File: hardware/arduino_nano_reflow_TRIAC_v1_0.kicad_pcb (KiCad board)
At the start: 2 copper layers, 100 x 50 mm, 36 parts, among them J1 AC IN 220v, J10 CONN_01X17, J11 CONN_01X03, J12 MOUNTING_HOLE, J13 MOUNTING_HOLE, J14 MOUNTING_HOLE, J15 MOUNTING_HOLE, J2 HEATER, J3 DC IN 12V, J4 12v FAN, J5 CONN_01X03, J6 CONN_01X03, J7 CONN_01X03, J8 CONN_01X03, J9 CONN_01X05, Q1 IRF540N, U1 MOC3020M

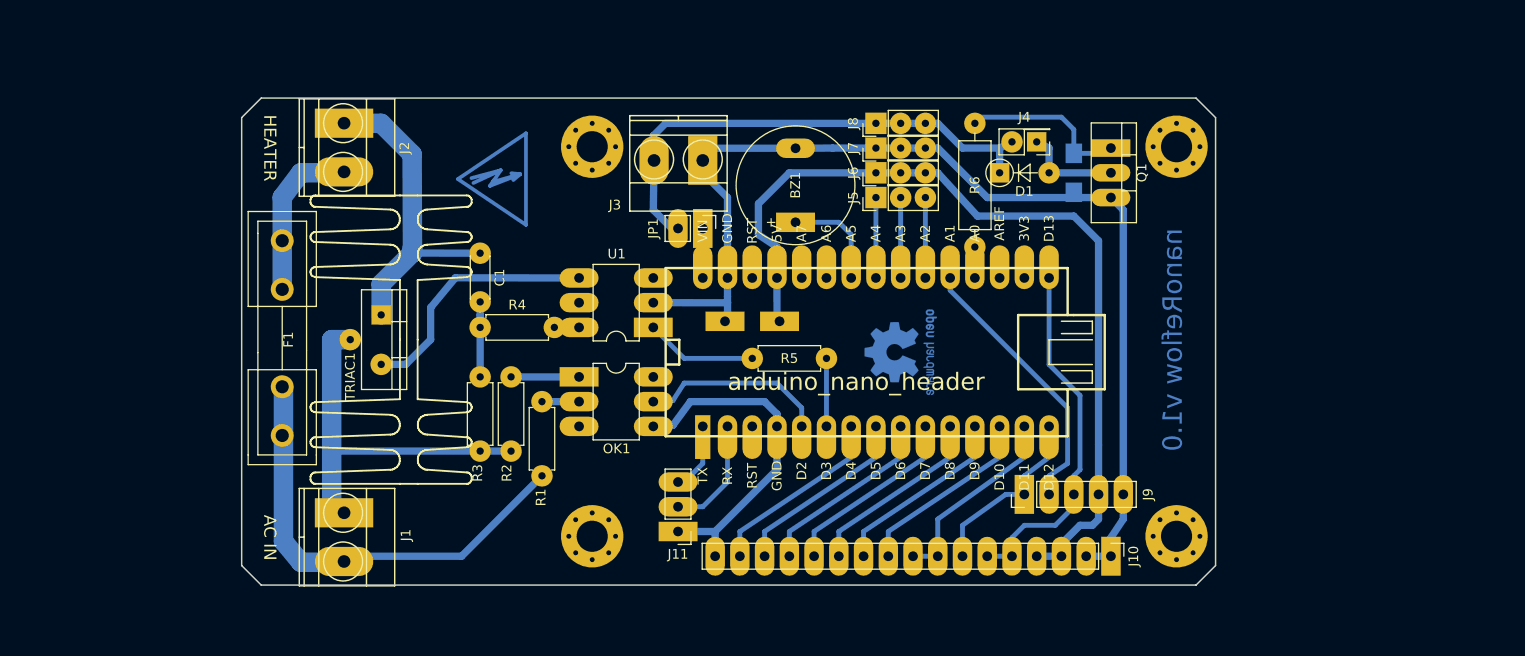
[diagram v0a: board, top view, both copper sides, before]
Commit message: Big update. Lots of schematic reorg and mostly final PCB layout. Updated zero crossing detector to be more accurate and added temp sensor on board instead of a connector to a separate module. Moved some pins around on the micro for better layout. Added safety ground to mains input.
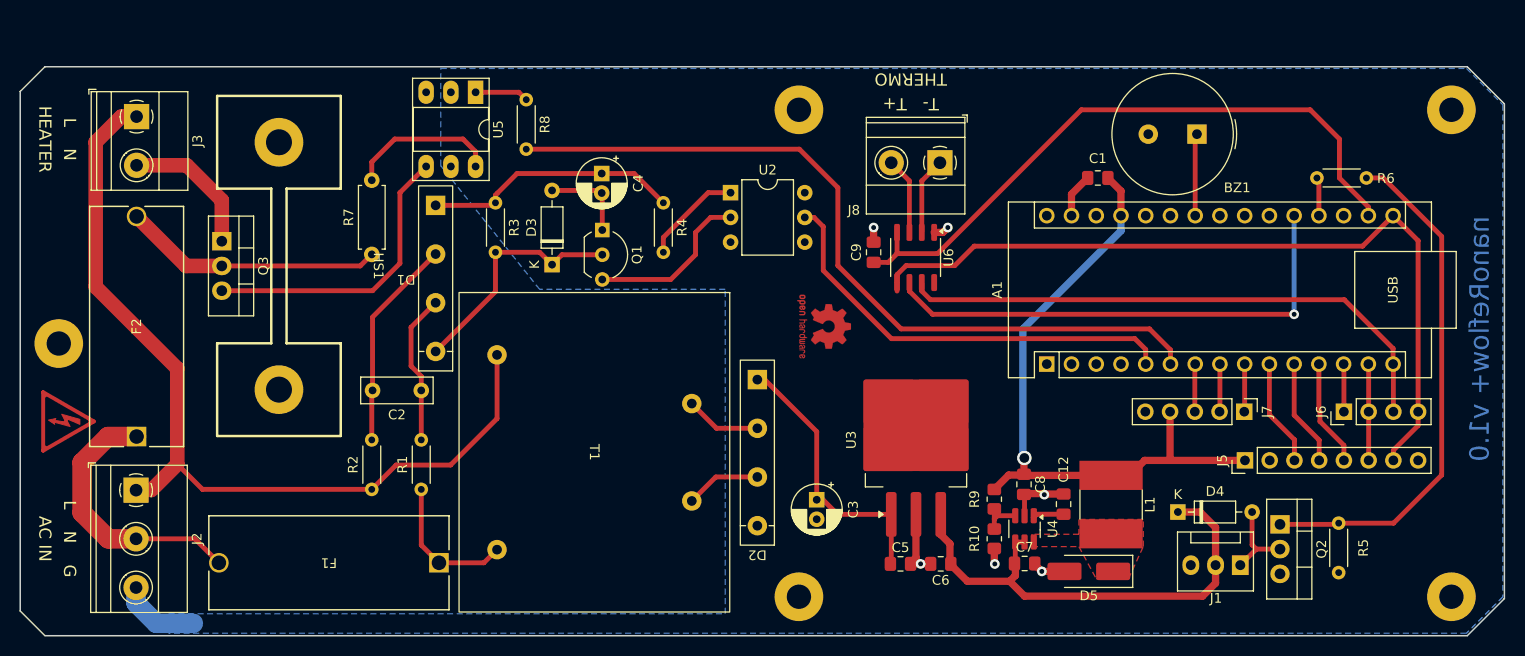
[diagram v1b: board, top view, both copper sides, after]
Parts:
- removed ARDUINO_NANO1: arduino_nano_header, local_modules:arduino_nano_header
- removed J10: CONN_01X17, Pin_Headers:Pin_Header_Straight_1x17_Pitch2.54mm
- removed J11: CONN_01X03, Pin_Headers:Pin_Header_Straight_1x03_Pitch2.54mm
- removed J12, J13, J14, J15: MOUNTING_HOLE, Mounting_Holes:MountingHole_3.2mm_M3_Pad_Via
- removed the J3 at (147.8, 74.4)
- removed J4: 12v FAN, Pin_Headers:Pin_Header_Straight_2x01_Pitch2.54mm
- removed J9: CONN_01X05, Pin_Headers:Pin_Header_Straight_1x05_Pitch2.54mm
- removed JP1: VIN enabler, Pin_Headers:Pin_Header_Straight_1x02_Pitch2.54mm
- removed KK1: TRIAC HEATSINK, local_modules:TO_220_heatsink
- removed OK1: H11AA1, Housings_DIP:DIP-6_W7.62mm_LongPads
- removed the R7 at (185.9, 75.7)
- removed U1: MOC3020M, Housings_DIP:DIP-6_W7.62mm_LongPads
- added A1: Arduino_Nano_Every, Module:Arduino_Nano, F.Cu at (183.2, 95.3)
- added C12: 0.01uF, Capacitor_SMD:C_0805_2012Metric_Pad1.18x1.45mm_HandSolder, F.Cu at (184.9, 109.7)
- added C3: 10uF, Capacitor_THT:CP_Radial_D5.0mm_P2.00mm, F.Cu at (159.5, 109.2)
- added C4: 10uF 10V, Capacitor_THT:CP_Radial_D5.0mm_P2.00mm, F.Cu at (137.5, 75.7)
- added C5: 0.22uF, Capacitor_SMD:C_0805_2012Metric_Pad1.18x1.45mm_HandSolder, F.Cu at (168.1, 115.8)
- added C6: 0.1uF, Capacitor_SMD:C_0805_2012Metric_Pad1.18x1.45mm_HandSolder, F.Cu at (172.3, 115.8)
- added C7: 0.1uF, Capacitor_SMD:C_0805_2012Metric_Pad1.18x1.45mm_HandSolder, F.Cu at (180.9, 115.8)
- added C8: 10uF, Capacitor_SMD:C_0805_2012Metric_Pad1.18x1.45mm_HandSolder, F.Cu at (180.8, 107.7)
- added C9: 0.1 uF 6.3 V, Capacitor_SMD:C_0805_2012Metric_Pad1.18x1.45mm_HandSolder, F.Cu at (165.4, 83.8)
- added D2: B40C1500A, arduino_nano_reflow:B40C, F.Cu at (153.5, 104.4)
- added D3: 1N4148, Diode_THT:D_DO-35_SOD27_P7.62mm_Horizontal, F.Cu at (132.4, 85.1)
- added D4: 1N4007, Diode_THT:D_DO-35_SOD27_P7.62mm_Horizontal, F.Cu at (196.6, 110.5)
- added D5: 40V, 2A, Diode_SMD:D_SMA_Handsoldering, F.Cu at (187.5, 116.6)
- added F1: 2A, arduino_nano_reflow:FUSE_0PTF0078P_LTF, F.Cu at (120.8, 115.7)
- added HS1: ~, arduino_nano_reflow:Aavid 51300 Heatsink, F.Cu at (103.5, 85.2)
- added J1: 12v FAN, Connector:FanPinHeader_1x03_P2.54mm_Vertical, F.Cu at (203.0, 116.0)
- added L1: 6 uH, 2.8A, arduino_nano_reflow:Bourns SRN6028C Inductor hand solder, F.Cu at (189.8, 109.7)
- added Q2: IRF540N, Package_TO_SOT_THT:TO-220-3_Vertical, F.Cu at (207.1, 111.8)
- added R10: 28k, Resistor_SMD:R_0805_2012Metric_Pad1.20x1.40mm_HandSolder, F.Cu at (177.8, 113.2)
- added R4: 1k, Resistor_THT:R_Axial_DIN0204_L3.6mm_D1.6mm_P5.08mm_Horizontal, F.Cu at (143.8, 78.7)
- added R8: 1k, Resistor_THT:R_Axial_DIN0204_L3.6mm_D1.6mm_P5.08mm_Horizontal, F.Cu at (129.7, 68.2)
- added R9: 49.9k, Resistor_SMD:R_0805_2012Metric_Pad1.20x1.40mm_HandSolder, F.Cu at (177.8, 109.2)
- added REF**: MountingHole_2.5mm_Pad, MountingHole:MountingHole_2.5mm_Pad, F.Cu at (157.7, 119.2)
- added REF**: MountingHole_2.5mm_Pad, MountingHole:MountingHole_2.5mm_Pad, F.Cu at (157.7, 69.2)
- added REF**: MountingHole_2.5mm_Pad, MountingHole:MountingHole_2.5mm_Pad, F.Cu at (224.7, 119.2)
- added REF**: MountingHole_2.5mm_Pad, MountingHole:MountingHole_2.5mm_Pad, F.Cu at (81.7, 93.2)
- added REF**: MountingHole_2.5mm_Pad, MountingHole:MountingHole_2.5mm_Pad, F.Cu at (224.7, 69.2)
- added T1: 12 V, arduino_nano_reflow:BV301S15010, F.Cu at (136.7, 104.4)
- added U2: H11AA1, Package_DIP:DIP-6_W7.62mm, F.Cu at (150.7, 77.7)
- added U3: LM340T-12/NOPB, Package_TO_SOT_SMD:TO-263-3_TabPin4, F.Cu at (169.7, 103.1)
- added U4: AP3211K, Package_TO_SOT_SMD:SOT-23-6_Handsoldering, F.Cu at (180.9, 112.2)
- added U5: MOC3020M, Package_DIP:DIP-6_W7.62mm_Socket_LongPads, F.Cu at (124.5, 67.4)
- added U6: ~, Package_SO:SO-8_3.9x4.9mm_P1.27mm, F.Cu at (169.7, 84.4)
- BZ1: value Buzzer -> ~; footprint Buzzers_Beepers:Buzzer_12x9.5RM7.6 -> Buzzer_Beeper:Buzzer_TDK_PS1240P02BT_D12.2mm_H6.5mm
- C1: value 10n -> 0.1uF, 10 V; footprint Capacitors_THT:C_Disc_D4.3mm_W1.9mm_P5.00mm -> Capacitor_SMD:C_0805_2012Metric_Pad1.18x1.45mm_HandSolder
- C2: value 100n -> 1nF 200 V; footprint Capacitors_SMD:C_1206_HandSoldering -> Capacitor_THT:C_Rect_L7.2mm_W2.5mm_P5.00mm_FKS2_FKP2_MKS2_MKP2; moved to F.Cu
- D1: value 1N4007 -> B40C1500A; footprint Diodes_THT:D_A-405_P5.08mm_Vertical_AnodeUp -> arduino_nano_reflow:B40C
- F2: renamed from F1; value Fuse -> 5A; footprint Fuse_Holders_and_Fuses:Fuseholder5x20_horiz_open_inline_Type-I -> arduino_nano_reflow:FUSE_0PTF0078P_LTF
- J2: renamed from J1; value AC IN 220v -> AC IN; footprint Connectors_Terminal_Blocks:TerminalBlock_Pheonix_MKDS1.5-2pol -> TerminalBlock_Phoenix:TerminalBlock_Phoenix_MKDS-1,5-3_1x03_P5.00mm_Horizontal
- J3: renamed from J2; footprint Connectors_Terminal_Blocks:TerminalBlock_Pheonix_MKDS1.5-2pol -> TerminalBlock_Phoenix:TerminalBlock_Phoenix_MKDS-1,5-2_1x02_P5.00mm_Horizontal
- J5: value CONN_01X03 -> LCD; footprint Pin_Headers:Pin_Header_Straight_1x03_Pitch2.54mm -> Connector_PinHeader_2.54mm:PinHeader_1x08_P2.54mm_Vertical
- J6: value CONN_01X03 -> SD; footprint Pin_Headers:Pin_Header_Straight_1x03_Pitch2.54mm -> Connector_PinHeader_2.54mm:PinHeader_1x04_P2.54mm_Vertical
- J7: value CONN_01X03 -> ENC; footprint Pin_Headers:Pin_Header_Straight_1x03_Pitch2.54mm -> Connector_PinHeader_2.54mm:PinHeader_1x05_P2.54mm_Vertical
- J8: value CONN_01X03 -> K-TYPE; footprint Pin_Headers:Pin_Header_Straight_1x03_Pitch2.54mm -> TerminalBlock_Phoenix:TerminalBlock_Phoenix_MKDS-1,5-2_1x02_P5.00mm_Horizontal
- Q1: value IRF540N -> 40V, 0.8A; footprint TO_SOT_Packages_THT:TO-220_Vertical -> Package_TO_SOT_THT:TO-92_Inline_Wide
- Q3: renamed from TRIAC1; value BT137 -> BTA308X; footprint local_modules:TO-220_Vertical_BT137 -> Package_TO_SOT_THT:TO-220-3_Vertical
- R1: renamed from R2; value 47k 0.6w -> 220k; footprint Resistors_THT:R_Axial_DIN0207_L6.3mm_D2.5mm_P7.62mm_Horizontal -> Resistor_THT:R_Axial_DIN0204_L3.6mm_D1.6mm_P5.08mm_Horizontal
- R2: renamed from R1; value 47k 0.6w -> 220k; footprint Resistors_THT:R_Axial_DIN0207_L6.3mm_D2.5mm_P7.62mm_Horizontal -> Resistor_THT:R_Axial_DIN0204_L3.6mm_D1.6mm_P5.08mm_Horizontal
- R3: value 2.4k -> 22k; footprint Resistors_THT:R_Axial_DIN0207_L6.3mm_D2.5mm_P7.62mm_Horizontal -> Resistor_THT:R_Axial_DIN0204_L3.6mm_D1.6mm_P5.08mm_Horizontal
- R5: value 1k -> 100k; footprint Resistors_THT:R_Axial_DIN0207_L6.3mm_D2.5mm_P7.62mm_Horizontal -> Resistor_THT:R_Axial_DIN0204_L3.6mm_D1.6mm_P5.08mm_Horizontal
- R6: value 4K7 -> 4.7k; footprint Resistors_THT:R_Axial_DIN0309_L9.0mm_D3.2mm_P12.70mm_Horizontal -> Resistor_THT:R_Axial_DIN0204_L3.6mm_D1.6mm_P5.08mm_Horizontal
- R7: renamed from R4; value 180R -> 180; footprint Resistors_THT:R_Axial_DIN0207_L6.3mm_D2.5mm_P7.62mm_Horizontal -> Resistor_THT:R_Axial_DIN0207_L6.3mm_D2.5mm_P7.62mm_Horizontal
- REF**: value Symbol_HighVoltage_Type2_CopperTop_VerySmall -> Symbol_HighVoltage_Triangle_6x6mm_Copper; footprint Symbols:Symbol_HighVoltage_Type2_CopperTop_VerySmall -> Symbol:Symbol_HighVoltage_Triangle_6x6mm_Copper; moved to F.Cu
- REF***: value OSHW-Logo2_9.8x8mm_Copper -> OSHW-Logo2_7.3x6mm_Copper; footprint Symbols:OSHW-Logo2_9.8x8mm_Copper -> Symbol:OSHW-Logo2_7.3x6mm_Copper; moved to F.Cu
- moved R5 64.1 mm to (213.1, 116.7), turned to 90 degrees
- moved C1 63.9 mm to (188.4, 76.2), turned to 180 degrees
- moved D1 58.9 mm to (120.4, 86.5), turned to 180 degrees
- moved J6 54.0 mm to (213.7, 100.2)
- moved Q1 52.9 mm to (137.5, 81.5)
- moved REF** 50.7 mm to (82.7, 101.2)
- moved J5 46.5 mm to (203.5, 105.2)
- moved J7 46.5 mm to (203.4, 100.2), turned to -90 degrees
- moved BZ1 42.2 mm to (198.6, 71.7), turned to 180 degrees
- moved R6 35.8 mm to (210.9, 76.2), turned to 0 degrees
- moved C2 34.7 mm to (118.9, 98.0), turned to 180 degrees
- moved F2 25.1 mm to (89.7, 102.7), turned to 90 degrees
- moved J2 21.5 mm to (89.7, 108.3)
- moved J3 21.3 mm to (89.7, 69.9)
- moved Q3 18.0 mm to (98.5, 82.7)
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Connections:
- BZ1 pad 1: /BUZZER -> Net-(A1-SCL/A5)
- C1 pad 1: AC1_OUT -> 5V
- C1 pad 2: /AC_CAP -> GND
- C2 pad 1: GND -> Net-(C2-Pad1)
- C2 pad 2: 5V -> Net-(C2-Pad2)
- D1 pad 1: 12v -> Net-(D1-+)
- D1 pad 2: /FAN_GND -> Net-(D1--)
- F2 pad 1: AC2_OUT -> AC_IN_L
- F2 pad 2: AC2_IN -> Net-(Q3-A2)
- J2 pad 1: AC1_IN -> AC_IN_N
- J2 pad 2: AC2_IN -> AC_IN_L
- J3 pad 1: AC1_OUT -> AC_IN_N
- J3 pad 2: AC2_OUT -> AC_OUT_L
- J5 pad 1: /A4 -> 5V
- J5 pad 2: /A3 -> GND
- J5 pad 3: /A2 -> /LCD_CS
- J6 pad 1: 5V -> /SD_CS
- J6 pad 2: 5V -> /MOSI
- J6 pad 3: 5V -> /MISO
- J7 pad 1: GND -> /ENC_CH_A
- J7 pad 2: GND -> /ENC_CH_B
- J7 pad 3: GND -> /ENC_SW
- J8 pad 1: 12v -> /T-
- J8 pad 2: 12v -> /T+
- Q1 pad 1: Net-(Q1-Pad1) -> Net-(D3-A)
- Q1 pad 2: /FAN_GND -> Net-(D1--)
- Q1 pad 3: GND -> Net-(Q1-C)
- Q3 pad 1: AC1_OUT -> AC_OUT_L
- Q3 pad 2: AC1_IN -> Net-(Q3-A2)
- Q3 pad 3: /MOC_AC2 -> Net-(Q3-G)
- R1 pad 1: AC1_IN -> Net-(T1-AB)
- R1 pad 2: /OC1 -> Net-(C2-Pad1)
- R2 pad 1: AC2 -> AC_IN_N
- R2 pad 2: /OC2 -> Net-(C2-Pad2)
- R3 pad 1: /AC_CAP -> Net-(D1-+)
- R3 pad 2: AC1_IN -> Net-(D1--)
- R5 pad 1: Net-(R5-Pad1) -> GND
- R5 pad 2: /DIMM_CTRL -> Net-(Q2-G)
- R6 pad 2: Net-(Q1-Pad1) -> Net-(Q2-G)
- R7 pad 1: /AC_CAP -> Net-(Q3-A2)
- R7 pad 2: /MOC_AC1 -> Net-(R7-Pad2)
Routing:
- net GND: track 146.0 -> 35.1 mm, vias 0 -> 6
- net AC_IN_N: track 0.00 -> 90.7 mm
- net /DIMM_CTRL: track 6.98 -> 80.8 mm
- net 3V3: track 0.00 -> 66.8 mm
- net Net-(Q2-G): track 0.00 -> 53.4 mm
- net /SCK: track 37.2 -> 82.4 mm
- net /MISO: track 19.9 -> 58.2 mm
- net AC1_IN: track 37.6 -> 0.00 mm
- net AC2_IN: track 34.9 -> 0.00 mm
- net AC1_OUT: track 34.4 -> 0.00 mm
- net Net-(Q3-G): track 0.00 -> 30.5 mm
- net Net-(D2-+): track 0.00 -> 28.7 mm
- net AC_IN_L: track 0.00 -> 28.0 mm
- net Net-(Q3-A2): track 0.00 -> 26.7 mm
- net Net-(D1-+): track 0.00 -> 26.4 mm
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- added copper zone on B.Cu, net GND
- added copper zone on F.Cu, net Net-(D5-K)
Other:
- board size 100 x 50 mm -> 152.4 x 58.4 mm
- rule pad_to_mask_clearance: 0.2 -> 0.1
- board text added: "L N"
- board text added: "L N G"
- board text added: "T- T+"
- board text added: "THERMO"
- board text added: "nanoReflow+ v1.0"
- board text removed: "nanoReflow v1.0"

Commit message: Some small changes I forgot in the last commit, and an updated BOM.
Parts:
- moved REF** 0.80 mm to (81.7, 94.0)

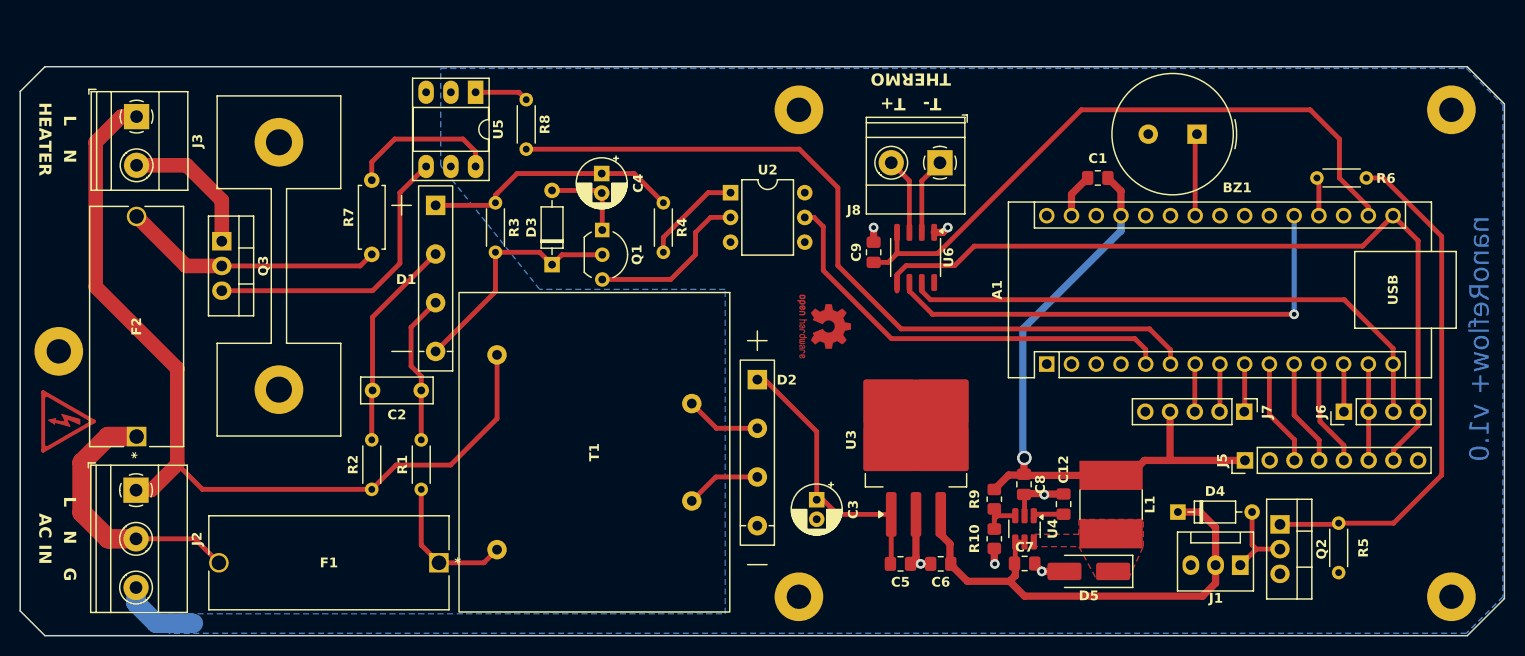
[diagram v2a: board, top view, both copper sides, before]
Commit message: Fixed grid in PCB, minor movement changes, and fixed DRC issues.
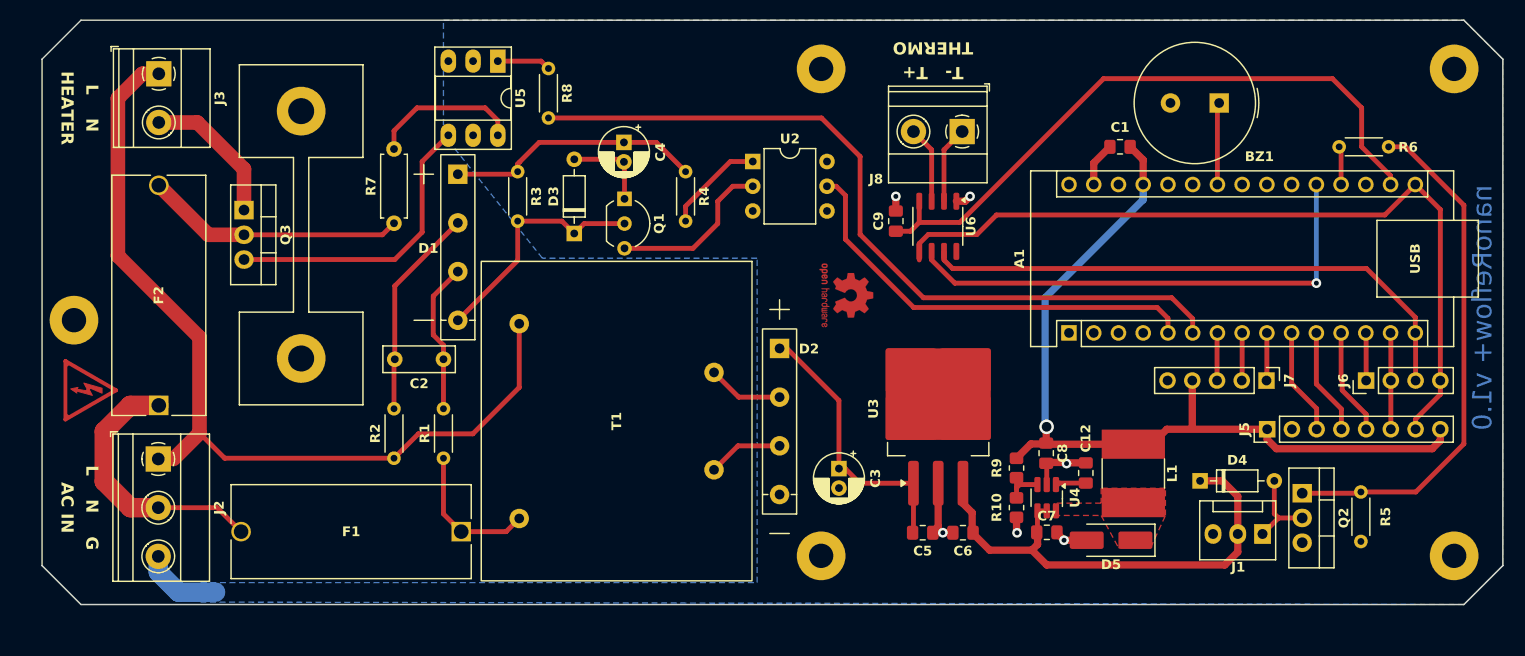
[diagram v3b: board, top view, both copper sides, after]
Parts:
- moved J3 4.96 mm to (92.0, 65.5)
- moved REF** 4.78 mm to (160.0, 115.0)
- moved REF** 4.78 mm to (160.0, 65.0)
- moved REF** 4.21 mm to (225.0, 115.0)
- moved REF** 4.21 mm to (225.0, 65.0)
- moved D1 3.93 mm to (122.7, 83.3)
- moved D2 3.93 mm to (155.7, 101.2)
- moved D4 3.93 mm to (198.9, 107.3)
- moved J1 3.93 mm to (205.3, 112.8)
- moved L1 3.93 mm to (192.1, 106.5)
- moved Q1 3.93 mm to (139.8, 78.3)
- moved R2 3.93 mm to (116.1, 105.0)
- moved R3 3.93 mm to (128.8, 75.5)
- moved R4 3.93 mm to (146.1, 75.5)
- moved R5 3.93 mm to (215.4, 113.5)
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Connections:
- REF** pad 1: (no net) -> GND (x3)
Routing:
- net 5V: track 67.1 -> 87.9 mm
- net AC_IN_N: track 90.7 -> 92.0 mm
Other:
- board size 152.4 x 58.4 mm -> 150 x 60 mm
